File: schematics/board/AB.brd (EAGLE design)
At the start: 78 x 21 mm, 65 parts

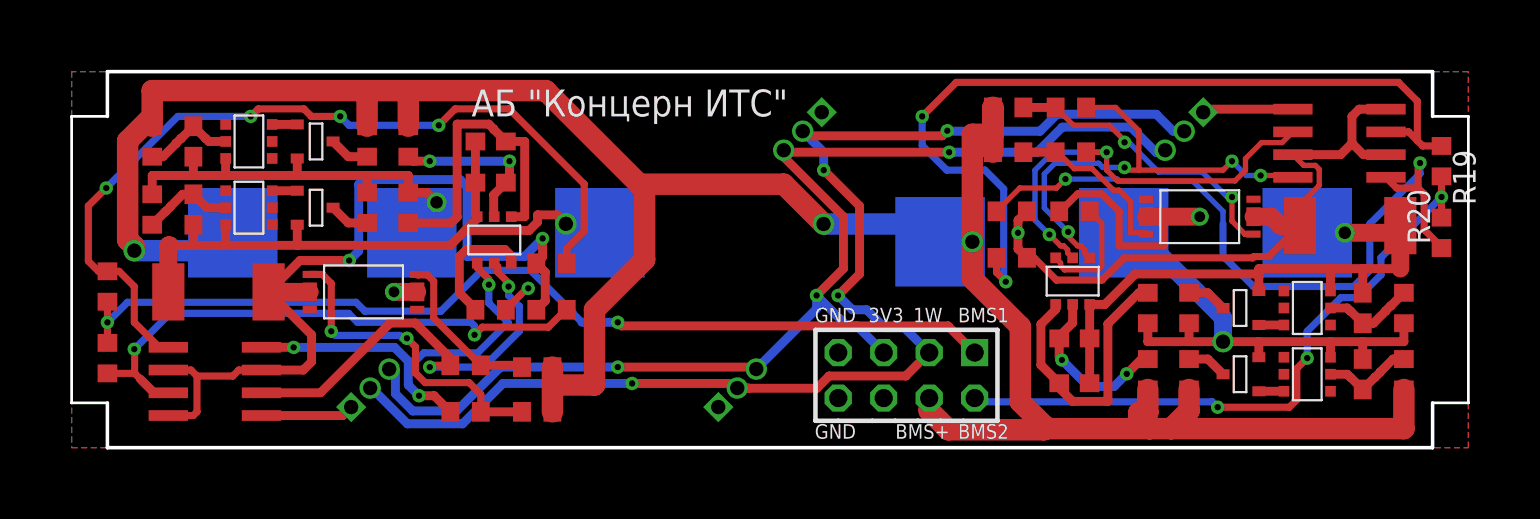
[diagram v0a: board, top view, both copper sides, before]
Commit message: Добавлены предохранители в библиотеку
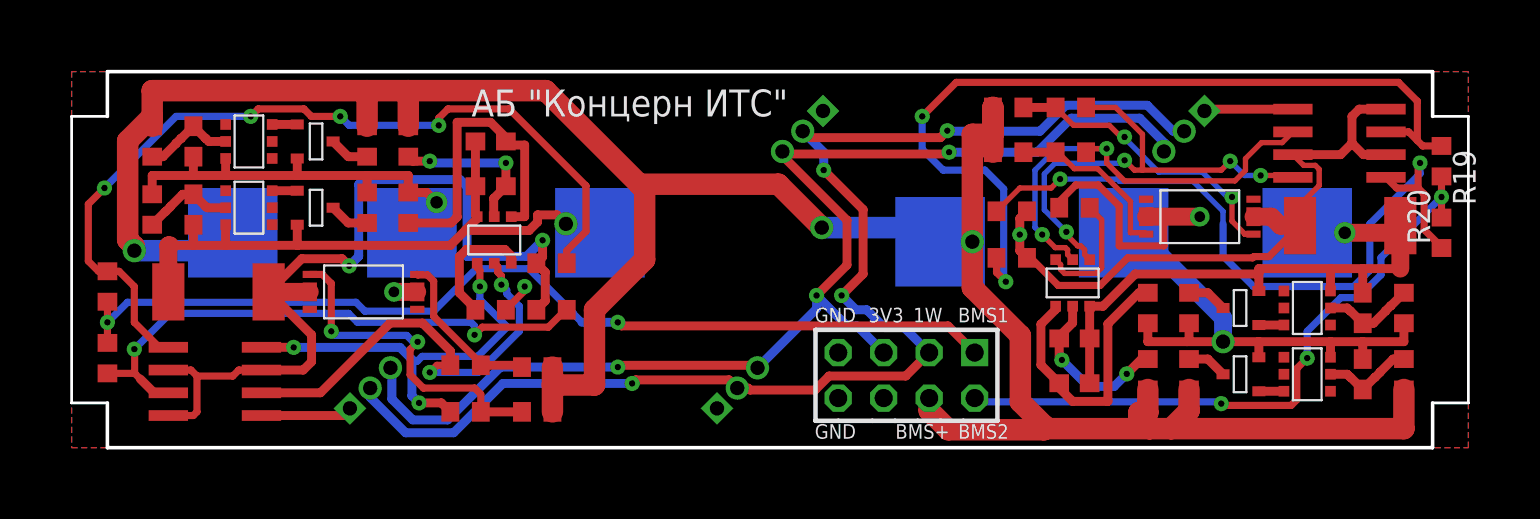
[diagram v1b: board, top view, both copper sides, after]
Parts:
- U$3, U$45: device CanCubeSat:HY2120 -> CanCubeSat:SOT23-6
- U$4, U$46, U$47, U$5: value HY2213 -> HY2213"; device CanCubeSat:HY2213 -> CanCubeSat:SOT23-6
- U$48, U$49, U$6, U$7: device CanCubeSat:SI2302CDS -> CanCubeSat:SOT23-3
- moved C1 0.20 mm to (23.4, 14.6)
- moved R49 0.20 mm to (56.0, 13.4)
- moved U$45 0.10 mm to (55.9, 9.20)
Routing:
- net 3V3: track 66.6 -> 68.0 mm
- net 1W: track 73.7 -> 75.0 mm
- net N$1: track 18.0 -> 18.8 mm

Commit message: Плата АB+DC-DC
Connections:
- net GND: now also R94.1, R95.1, R98.1, R99.1, U$10.2, U$10.4, U$2.2, U$2.4
- net NO_GND1: no longer R94.1, R95.1, U$2.2, U$2.4
- net NO_GND2: no longer R98.1, R99.1, U$10.2, U$10.4
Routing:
- net NO_GND1: track 48.8 -> 10.2 mm, vias 2 -> 0
- net NO_GND2: track 37.7 -> 8.21 mm, vias 1 -> 0
- net GND: track 27.0 -> 54.1 mm
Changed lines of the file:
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@@
 </element>
 <element name="R19" library="resistor" library_urn="urn:adsk.eagle:library:348" package="R0603" package3d_urn="urn:adsk.eagle:package:23555/3" value="2k26" x="76.5" y="16" smashed="yes" rot="R270">
-<attribute name="NAME" x="77.135" y="16.635" size="1.27" layer="25" rot="R270"/>
 <attribute name="VALUE" x="74.595" y="16.635" size="1.27" layer="27" rot="R270"/>
 </element>
@@
 <wire x1="63.361" y1="18.905" x2="63.25936875" y2="18.80336875" width="0.5" layer="1"/>
 <via x="25.3" y="9" extent="1-16" drill="0.35"/>
-<wire x1="24.25" y1="7.7" x2="24.25" y2="7.72116875" width="0.4" layer="1"/>
-<wire x1="25.3" y1="9" x2="25.3" y2="8.77116875" width="0.4" layer="1"/>
-<wire x1="25.3" y1="8.77116875" x2="24.25" y2="7.72116875" width="0.4" layer="1"/>
 <wire x1="56.07603125" y1="14.67" x2="55.15" y2="13.74396875" width="0.4" layer="1"/>
 <wire x1="55.15" y1="13.4" x2="55.15" y2="13.74396875" width="0.4" layer="1"/>
@@
 <wire x1="61" y1="11.27" x2="61" y2="12.9" width="0.4" layer="1"/>
 <wire x1="56.07603125" y1="14.67" x2="57.32396875" y2="14.67" width="0.4" layer="1"/>
+<contactref element="U$2" pad="2"/>
+<contactref element="U$2" pad="4"/>
+<contactref element="R95" pad="1"/>
+<contactref element="R94" pad="1"/>
+<wire x1="25.95" y1="10.3" x2="26.45" y2="9.8" width="0.5" layer="1"/>
+<wire x1="26.45" y1="9.8" x2="26.45" y2="9" width="0.5" layer="1"/>
+<wire x1="26.45" y1="9" x2="26.45" y2="8.2" width="0.5" layer="1"/>
+<wire x1="26.45" y1="8.2" x2="25.95" y2="7.7" width="0.5" layer="1"/>
+<contactref element="U$10" pad="2"/>
+<contactref element="U$10" pad="4"/>
+<contactref element="R98" pad="1"/>
+<contactref element="R99" pad="1"/>
+<wire x1="53.35" y1="13.2" x2="52.95" y2="12.8" width="0.5" layer="1"/>
+<wire x1="52.95" y1="12.8" x2="52.95" y2="11" width="0.5" layer="1"/>
+<wire x1="52.95" y1="11" x2="53.35" y2="10.6" width="0.5" layer="1"/>
+<wire x1="25.3" y1="9" x2="26.45" y2="9" width="0.5" layer="1"/>
+<wire x1="24.25" y1="7.7" x2="25.95" y2="7.7" width="0.5" layer="1"/>
+<wire x1="53.35" y1="13.2" x2="53.55" y2="13.4" width="0.5" layer="1"/>
+<wire x1="53.55" y1="13.4" x2="55.15" y2="13.4" width="0.5" layer="1"/>
+<wire x1="5.4" y1="4.335" x2="6.665" y2="4.335" width="0.5" layer="1"/>
+<wire x1="7" y1="4" x2="6.665" y2="4.335" width="0.5" layer="1"/>
+<wire x1="5.4" y1="1.795" x2="6.795" y2="1.795" width="0.5" layer="1"/>
+<wire x1="6.795" y1="1.795" x2="7" y2="2" width="0.5" layer="1"/>
+<wire x1="7" y1="2" x2="7" y2="4" width="0.5" layer="1"/>
+<wire x1="10.6" y1="1.795" x2="7.205" y2="1.795" width="0.5" layer="1"/>
+<wire x1="7.205" y1="1.795" x2="7" y2="2" width="0.5" layer="1"/>
+<wire x1="73.4" y1="16.365" x2="72.135" y2="16.365" width="0.5" layer="1"/>
+<wire x1="71.83" y1="16.67" x2="72.135" y2="16.365" width="0.5" layer="1"/>
+<wire x1="73.4" y1="18.905" x2="72.405" y2="18.905" width="0.5" layer="1"/>
+<wire x1="72.405" y1="18.905" x2="71.83" y2="18.33" width="0.5" layer="1"/>
+<wire x1="71.83" y1="18.33" x2="71.83" y2="16.67" width="0.5" layer="1"/>
+<wire x1="68.2" y1="18.905" x2="71.255" y2="18.905" width="0.5" layer="1"/>
+<wire x1="71.255" y1="18.905" x2="71.83" y2="18.33" width="0.5" layer="1"/>
 </signal>
 <signal name="B-1">
@@
 <wire x1="12.935" y1="4.335" x2="10.6" y2="4.335" width="0.5" layer="1"/>
 <wire x1="13.4" y1="4.8" x2="12.935" y2="4.335" width="0.5" layer="1"/>
-<contactref element="U$2" pad="2"/>
-<contactref element="U$2" pad="4"/>
-<contactref element="R95" pad="1"/>
-<contactref element="R94" pad="1"/>
-<wire x1="25.95" y1="10.3" x2="26.45" y2="9.8" width="0.5" layer="1"/>
-<wire x1="26.45" y1="9.8" x2="26.45" y2="8.2" width="0.5" layer="1"/>
-<wire x1="26.45" y1="8.2" x2="25.95" y2="7.7" width="0.5" layer="1"/>
-<wire x1="5.4" y1="1.795" x2="6.795" y2="1.795" width="0.4" layer="1"/>
-<wire x1="6.795" y1="1.795" x2="7" y2="2" width="0.4" layer="1"/>
-<wire x1="6.665" y1="4.335" x2="7" y2="4" width="0.4" layer="1"/>
-<wire x1="6.665" y1="4.335" x2="5.4" y2="4.335" width="0.4" layer="1"/>
-<wire x1="7" y1="2" x2="7" y2="4" width="0.4" layer="1"/>
-<wire x1="7" y1="4" x2="9" y2="4" width="0.4" layer="1"/>
-<wire x1="9" y1="4" x2="9.335" y2="4.335" width="0.4" layer="1"/>
-<wire x1="9.335" y1="4.335" x2="10.6" y2="4.335" width="0.4" layer="1"/>
-<wire x1="11" y1="8.7" x2="12.8518" y2="10.5518" width="0.5" layer="1"/>
-<wire x1="15.1" y1="10.5518" x2="12.8518" y2="10.5518" width="0.5" layer="1"/>
-<wire x1="15.1" y1="10.5518" x2="15.5" y2="10.1518" width="0.5" layer="1"/>
-<via x="15.5" y="10.1518" extent="1-16" drill="0.35"/>
-<via x="26.3" y="11.5818" extent="1-16" drill="0.35"/>
-<wire x1="16.03" y1="14.69468125" x2="16.30531875" y2="14.97" width="0.5" layer="16"/>
-<wire x1="16.30531875" y1="14.97" x2="21.69468125" y2="14.97" width="0.5" layer="16"/>
-<wire x1="15.5" y1="10.1518" x2="16.03" y2="10.6818" width="0.5" layer="16"/>
-<wire x1="16.03" y1="10.6818" x2="16.03" y2="14.69468125" width="0.5" layer="16"/>
-<wire x1="21.69468125" y1="14.97" x2="22.082340625" y2="14.582340625" width="0.5" layer="16"/>
-<wire x1="22.082340625" y1="14.582340625" x2="22.082340625" y2="10.6818" width="0.5" layer="16"/>
-<wire x1="25.4" y1="10.6818" x2="22.082340625" y2="10.6818" width="0.5" layer="16"/>
-<wire x1="25.4" y1="10.6818" x2="26.3" y2="11.5818" width="0.5" layer="16"/>
-<wire x1="26.3" y1="11.5818" x2="26.3" y2="10.65" width="0.5" layer="1"/>
-<wire x1="26.3" y1="10.65" x2="25.95" y2="10.3" width="0.5" layer="1"/>
 </signal>
 <signal name="N$10">
@@
 <wire x1="69.67" y1="14.64174375" x2="68.6" y2="13.57174375" width="0.3" layer="1"/>
 <wire x1="68.2" y1="16.365" x2="68.8" y2="15.765" width="0.3" layer="1"/>
-<contactref element="U$10" pad="2"/>
-<contactref element="U$10" pad="4"/>
-<contactref element="R98" pad="1"/>
-<contactref element="R99" pad="1"/>
-<wire x1="53.35" y1="13.2" x2="52.95" y2="12.8" width="0.5" layer="1"/>
-<wire x1="52.95" y1="12.8" x2="52.95" y2="11.9" width="0.5" layer="1"/>
-<wire x1="52.95" y1="11.9" x2="52.95" y2="11" width="0.5" layer="1"/>
-<wire x1="52.95" y1="11" x2="53.35" y2="10.6" width="0.5" layer="1"/>
-<via x="52.95" y="11.9" extent="1-16" drill="0.35"/>
-<wire x1="73.4" y1="18.905" x2="71.905" y2="18.905" width="0.5" layer="1"/>
-<wire x1="71.905" y1="18.905" x2="71.5" y2="18.5" width="0.5" layer="1"/>
-<wire x1="71.5" y1="18.5" x2="71.5" y2="17" width="0.5" layer="1"/>
-<wire x1="72.135" y1="16.365" x2="73.4" y2="16.365" width="0.5" layer="1"/>
-<wire x1="71.5" y1="17" x2="72.135" y2="16.365" width="0.5" layer="1"/>
-<wire x1="68.2" y1="16.365" x2="70.865" y2="16.365" width="0.5" layer="1"/>
-<wire x1="70.865" y1="16.365" x2="71.5" y2="17" width="0.5" layer="1"/>
-<wire x1="68.6" y1="12.4" x2="66.87" y2="10.67" width="0.4" layer="1"/>
-<wire x1="66.87" y1="10.67" x2="66.022475" y2="10.67" width="0.4" layer="1"/>
-<wire x1="66.022475" y1="10.67" x2="65.952475" y2="10.6" width="0.4" layer="1"/>
-<wire x1="65.952475" y1="10.6" x2="58.9793625" y2="10.6" width="0.4" layer="1"/>
-<wire x1="53.55603125" y1="10.6" x2="53.35" y2="10.6" width="0.4" layer="1"/>
-<wire x1="58.9793625" y1="10.6" x2="57.4393625" y2="9.06" width="0.4" layer="1"/>
-<wire x1="57.4393625" y1="9.06" x2="55.09603125" y2="9.06" width="0.4" layer="1"/>
-<wire x1="55.09603125" y1="9.06" x2="53.55603125" y2="10.6" width="0.4" layer="1"/>
 </signal>
 <signal name="N$13">

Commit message: Готова плата RADIO и переделана плата AB
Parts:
- removed R15, R16: 100R, resistor:R0603
- removed R17, R18: 100k, resistor:R0603
- removed R19, R20: 2k26, resistor:R0603
- removed R98, R99: 200k, resistor:R0603
- removed U$10: MOCD217M, CanCubeSat:SOIC8
- removed U$26: FS8205A-, CanCubeSat:FS8205A-
- added R21, R22: 200k, resistor:R0603
- added R23, R24: 150R, resistor:R0603
- added R25, R26: 10k, resistor:R0603
- added R27, R28: 2k26, resistor:R0603
- added U$11: MOCD217M, CanCubeSat:SOIC8
- added U$12, U$13, U$8, U$9: IRF7905PBF, CanCubeSat:SO8
- DS18B20, DS18B20A, DS18B20B, DS18B20C: value CONNECT1X3 -> DS18B20
- R10, R9: value 100R -> 150R
- R11, R12: value 100k -> 10k
- U$1: value FS8205A- -> PCB-"Storage Battery"; device CanCubeSat:FS8205A- -> CanCubeSat:ITS-LOGO
- moved U$1 38.1 mm to (24.9, 13.3), turned to 0 degrees
- moved R14 32.6 mm to (34.0, 2.80)
- moved R13 32.0 mm to (34.0, 5.90)
- moved C1 19.4 mm to (4.50, 19.1)
- moved U$2 19.0 mm to (27.0, 4.30), turned to 90 degrees
- moved C2 18.9 mm to (4.50, 17.0)
- moved C25 18.0 mm to (73.5, 1.90)
- moved C26 17.5 mm to (73.5, 4.00)
- moved U$3 16.6 mm to (8.20, 17.9), turned to 180 degrees
- moved R6 16.0 mm to (4.50, 1.10), turned to 180 degrees
- moved R54 15.8 mm to (73.5, 19.9), turned to 0 degrees
- moved R1 15.5 mm to (12.8, 19.0), turned to 0 degrees
- moved U$45 15.2 mm to (69.8, 3.10), turned to 0 degrees
- moved R49 14.6 mm to (65.2, 2.00), turned to 180 degrees
- moved R2 14.5 mm to (4.50, 14.9), turned to 180 degrees
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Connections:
- removed net N$10: R16.1, R17.2, U$1.5
- removed net N$14: R15.1, R18.1, U$1.4
- removed net N$19: R19.1, R99.2, U$10.3
- removed net N$3 (its old number): R20.1, R98.2, U$10.1
- new net N$16: U$9.5, U$9.6, U$9.7, U$9.8
- new net N$17: R10.1, U$2.8
- new net N$20: R22.2, R27.1, U$11.3
- new net N$21: U$8.5, U$8.6, U$8.7, U$8.8
- new net N$22: R9.1, U$2.6
- new net N$23: R12.1, R9.2, U$8.4
- new net N$24: R21.2, R28.1, U$11.1
- new net N$26: R24.2, R25.2, U$12.2
- new net N$27: R24.1, U$11.8
- new net N$28: R23.1, U$11.6
- new net N$29: R23.2, R26.1, U$12.4
- new net N$30: U$11.7, U$12.1, U$13.1
- new net N$31: U$13.5, U$13.6, U$13.7, U$13.8
- new net N$32: U$12.5, U$12.6, U$12.7, U$12.8
- net BMS+: now also R25.1, R26.2; no longer R17.1, R18.2
- net BMS2: now also R27.2, R28.2; no longer R19.2, R20.2
- net GND: now also R21.1, R22.1, U$11.2, U$11.4, U$11.5, U$12.3, U$8.3; no longer R1.1, R49.1, R98.1, R99.1, U$1.23, U$10.2, U$10.4, U$10.5, U$26.23
- net N$1: now also U$2.7, U$8.1, U$9.1; no longer R10.1, R11.2, U$26.5
- net N$2: now also R10.2, R11.2, U$8.2; no longer R12.1, R9.1, U$26.4
- net NO_GND1: now also R1.1, U$9.3; no longer U$2.7, U$26.67
- net NO_GND2: now also R49.1, U$13.3; no longer U$1.67, U$10.7
- net OC1: now also U$9.2; no longer R9.2, U$2.6
- net OC2: now also U$13.2; no longer R15.2, U$10.6
- net OD1: now also U$9.4; no longer R10.2, U$2.8
- net OD2: now also U$13.4; no longer R16.2, U$10.8
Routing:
- net GND: track 54.1 -> 129.2 mm, vias 3 -> 0
- net N$19: track 48.6 -> 0.00 mm, vias 2 -> 0
- net N$25: track 48.4 -> 4.92 mm, vias 4 -> 0
- net N$3 (its old number): track 40.4 -> 0.00 mm, vias 2 -> 0
- net BMS1: track 54.3 -> 25.9 mm, vias 2 -> 0
- net N$30: track 0.00 -> 28.1 mm, vias 0 -> 2
- net N$18: track 31.6 -> 4.45 mm, vias 2 -> 0
- net N$26: track 0.00 -> 24.6 mm, vias 0 -> 2
- net B-1: track 36.8 -> 60.5 mm, vias 1 -> 6
- net BMS+: track 145.5 -> 166.9 mm, vias 3 -> 4
- net OD2: track 26.7 -> 9.85 mm, vias 4 -> 0
- net N$23: track 0.00 -> 16.7 mm, vias 0 -> 2
- net N$10: track 16.7 -> 0.00 mm, vias 2 -> 0
- net OC1: track 25.3 -> 10.0 mm, vias 2 -> 0
- net OC2: track 25.1 -> 10.3 mm, vias 2 -> 0
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- added copper zone on layer 1, net B-1
- added copper zone on layer 1, net B-2
- added copper zone on layer 16, net B-2
- added copper zone on layer 16, net BMS+
- added copper zone on layer 1, net GND
- added copper zone on layer 1, net N$1
- added copper zone on layer 1, net N$16
- added copper zone on layer 1, net N$21
- added copper zone on layer 1, net N$30
- added copper zone on layer 1, net N$31
- added copper zone on layer 1, net N$32
- added copper zone on layer 1, net NO_GND1
- added copper zone on layer 1, net NO_GND2
- removed copper zone on layer 1, net BMS+
- removed copper zone on layer 16, net GND
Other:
- board text added: "HY2120"
- board text added: "HY2213"
- board text added: "IRF7905"
- board text added: "SI2302"
- board text removed: "АБ "Концерн ИТС""
